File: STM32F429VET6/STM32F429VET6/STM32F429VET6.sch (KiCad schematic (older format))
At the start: 0 parts

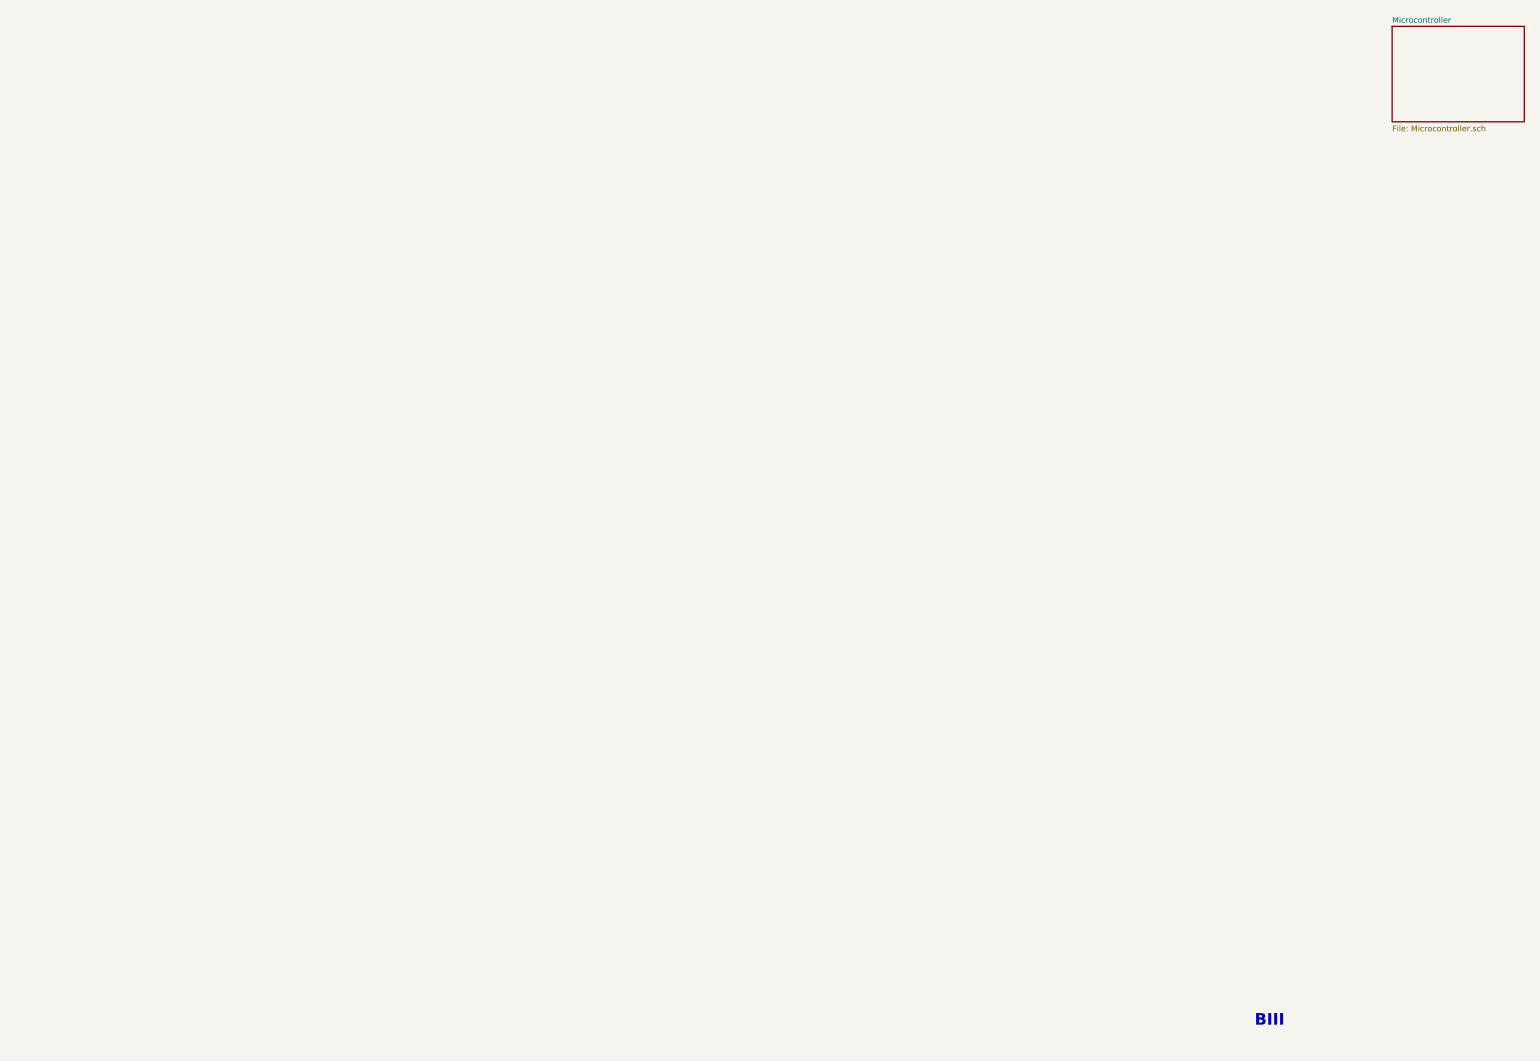
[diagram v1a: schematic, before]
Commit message: Completed Power Section
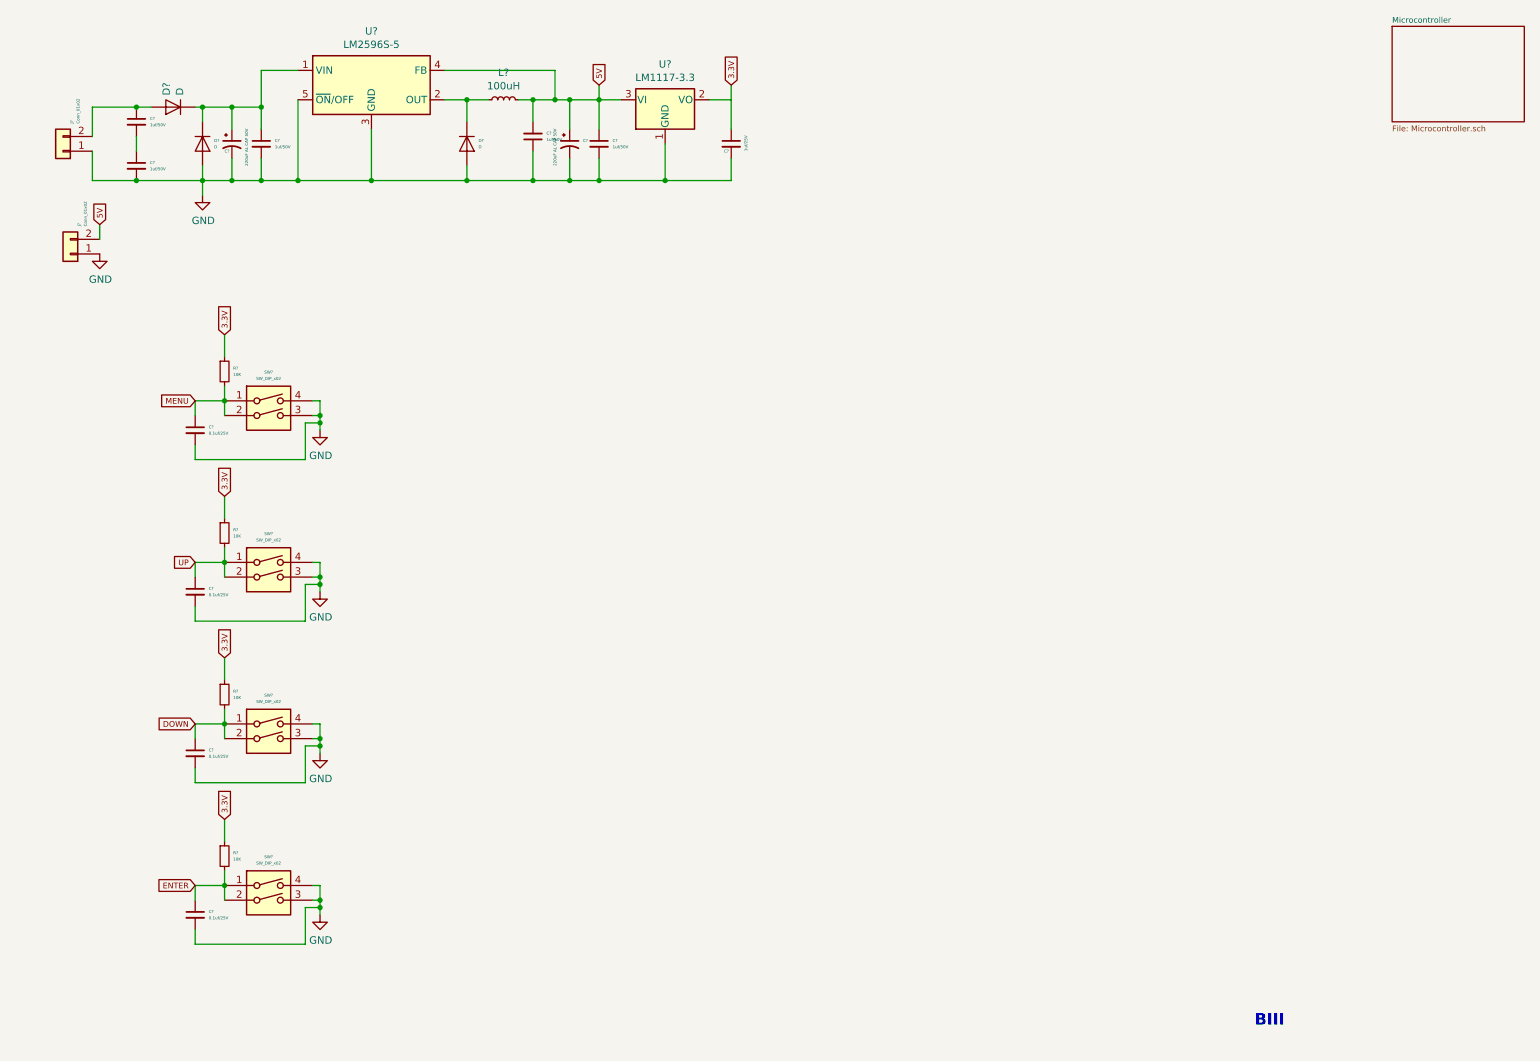
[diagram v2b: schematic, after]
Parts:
- added C? (x5): 1uf/50V, Capacitor_SMD:C_0805_2012Metric_Pad1.15x1.40mm_HandSolder, symbol Device:C_Small
- added C? (x2): 220uF AL CAP 50V, Capacitor_SMD:CP_Elec_4x4.5, symbol Device:CP1_Small
- added C?: 1uf/25V, Capacitor_SMD:C_0805_2012Metric_Pad1.15x1.40mm_HandSolder, symbol Device:C_Small
- added C? (x4): 0.1uf/25V, Capacitor_SMD:C_0805_2012Metric_Pad1.15x1.40mm_HandSolder, symbol Device:C_Small
- added D? (x3): D, symbol Device:D
- added J? (x2): Conn_01x02, Connector_PinHeader_2.54mm:PinHeader_1x02_P2.54mm_Vertical, symbol Connector_Generic:Conn_01x02
- added L?: 100uH, symbol Device:L_Small
- added R? (x4): 10K, Resistor_SMD:R_0805_2012Metric_Pad1.15x1.40mm_HandSolder, symbol Device:R_Small
- added SW? (x4): SW_DIP_x02, Button_Switch_SMD:SW_SPST_B3S-1000, symbol Switch:SW_DIP_x02
- added U?: LM2596S-5, Package_TO_SOT_SMD:TO-263-5_TabPin3, symbol Regulator_Switching:LM2596S-5
- added U?: LM1117-3.3, symbol Regulator_Linear:LM1117-3.3
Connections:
- new net: C?.1, D?.2 (A), J?.2 (Pin_2)
- new net: C?.1, C?.2
- new net: C?.1, C?.1, D?.1 (K), D?.1 (K), U?.1 (VIN)
- new net: D?.1 (K), L?.1, U?.2 (OUT)
- new net 3.3V: C?.1, R?.1, R?.1, R?.1, R?.1, U?.2 (VO)
- new net 5V: C?.1, C?.1, C?.2, J?.2 (Pin_2), L?.2, U?.3 (VI), U?.4 (FB)
- new net DOWN: C?.1, R?.2, SW?.1, SW?.2
- new net ENTER: C?.1, R?.2, SW?.1, SW?.2
- new net GND: C?.1, C?.2, C?.2, C?.2, C?.2, C?.2, C?.2, C?.2, C?.2, C?.2, C?.2, D?.2 (A), D?.2 (A), J?.1 (Pin_1), J?.1 (Pin_1), SW?.3, SW?.3, SW?.3, SW?.3, SW?.4, SW?.4, SW?.4, SW?.4, U?.1 (GND), U?.3 (GND), U?.5 (~ON~/OFF)
- new net MENU: C?.1, R?.2, SW?.1, SW?.2
- new net UP: C?.1, R?.2, SW?.1, SW?.2

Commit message: Completed 2 sections
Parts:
- added C?: 0.1uf/25V, Capacitor_SMD:C_0805_2012Metric_Pad1.15x1.40mm_HandSolder, symbol Device:C_Small
- added J?: Conn_01x03, symbol Connector_Generic:Conn_01x03
- added R? (x7): 10K, Resistor_SMD:R_0805_2012Metric_Pad1.15x1.40mm_HandSolder, symbol Device:R_Small
- added R? (x4): 100E, Resistor_SMD:R_0805_2012Metric_Pad1.15x1.40mm_HandSolder, symbol Device:R_Small
- added R? (x4): 10R, Resistor_SMD:R_0805_2012Metric_Pad1.15x1.40mm_HandSolder, symbol Device:R_Small
- added SW? (x12): SW_DIP_x02, Button_Switch_SMD:SW_SPST_B3S-1000, symbol Switch:SW_DIP_x02
- added U?: SN65HVD485ED, SN65HVD485ED:SN65HVD485ED, symbol SN65HVD485ED:SN65HVD485ED
- added U?: D5V0L2B3SO-7, D5V0L2B3SO7:D5V0L2B3SO-7, symbol D5V0L2B3SO7:D5V0L2B3SO-7
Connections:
- net 3.3V: now also R?.1, R?.1, R?.1, R?.1
- net 5V: now also C?.1, R?.1, R?.2, U?.8 (VCC)
- net GND: now also C?.2, J?.1 (Pin_1), R?.2, R?.2, U?.3 (EPAD), U?.5 (GND)
- new net: R?.1, R?.2, SW?.1, SW?.1, SW?.1, SW?.2, SW?.2, SW?.2 (x4)
- new net: R?.1, U?.6 (A)
- new net: R?.1, U?.7 (B)
- new net: J?.3 (Pin_3), R?.1, R?.1, R?.2, U?.1 (EPAD)
- new net: J?.2 (Pin_2), R?.1, R?.2, R?.2, U?.2 (EPAD)
- new net SW_CO1: SW?.3, SW?.3, SW?.3, SW?.3, SW?.4, SW?.4, SW?.4, SW?.4
- new net SW_CO2: SW?.3, SW?.3, SW?.3, SW?.3, SW?.4, SW?.4, SW?.4, SW?.4
- new net SW_CO3: SW?.3, SW?.3, SW?.3, SW?.3, SW?.4, SW?.4, SW?.4, SW?.4
- new net SW_RW1: R?.2
- new net SW_RW2: R?.2
- new net SW_RW3: R?.2
- new net SW_RW4: R?.2
- new net USART2_DE: R?.1, U?.2 (*RE), U?.3 (DE)
- new net USART2_RX: R?.2, U?.1 (R)
- new net USART2_TX: U?.4 (D)
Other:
- moved on the sheet: C?, R?, SW?

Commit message: Completed 3 pages
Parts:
- added C?: 0.1uf/25V, Capacitor_SMD:C_0805_2012Metric_Pad1.15x1.40mm_HandSolder, symbol Device:C_Small
- added R?: 10K, Resistor_SMD:R_0805_2012Metric_Pad1.15x1.40mm_HandSolder, symbol Device:R_Small
- added U?: T80-75HCP, symbol T80-75HCP:T80-75HCP
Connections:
- net 3.3V: now also C?.1, R?.1, U?.3 (WP#), U?.5 (VCC), U?.6 (HOLD)
- net GND: now also C?.2, U?.4 (VSS)
- new net SERIAL_FLASH_CLK: U?.7 (CLK)
- new net SERIAL_FLASH_CS: R?.2, U?.1 (CS#)
- new net SERIAL_FLASH_MISO: U?.2 (DO)
- new net SERIAL_FLASH_MOSI: U?.8 (DI)
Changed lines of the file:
@@
 	9700 3250 9200 3250
 Connection ~ 9200 3250
+$Comp
+L T80-75HCP:T80-75HCP U?
+U 1 1 5FD75780
+P 8500 5150
+F 0 "U?" H 8500 5475 50  0000 C CNN
+F 1 "T80-75HCP" H 8500 5384 50  0000 C CNN
+F 2 "" H 8500 5150 50  0001 C CNN
+F 3 "" H 8500 5150 50  0001 C CNN
+	1    8500 5150
+	1    0    0    -1
+$EndComp
+Wire Wire Line
+	7800 4850 7800 4800
+Text GLabel 7800 4700 1    39   Input ~ 0
+3.3V
+$Comp
+L Device:R_Small R?
+U 1 1 5FD84F8C
+P 7800 4950
+AR Path="/5FD5E119/5FD84F8C" Ref="R?"  Part="1"
+AR Path="/5FD84F8C" Ref="R?"  Part="1"
+F 0 "R?" H 7859 4972 20  0000 L CNN
+F 1 "10K" H 7859 4929 20  0000 L CNN
+F 2 "Resistor_SMD:R_0805_2012Metric_Pad1.15x1.40mm_HandSolder" H 7800 4950 50  0001 C CNN
+F 3 "~" H 7800 4950 50  0001 C CNN
+	1    7800 4950
+	1    0    0    -1
+$EndComp
+Wire Wire Line
+	8200 5050 7800 5050
+Text GLabel 8800 5350 2    39   Input ~ 0
+SERIAL_FLASH_MOSI
+Text GLabel 7500 5150 0    39   Input ~ 0
+SERIAL_FLASH_MISO
+Text GLabel 8800 5250 2    39   Input ~ 0
+SERIAL_FLASH_CLK
+Text GLabel 7450 5050 0    39   Input ~ 0
+SERIAL_FLASH_CS
+Wire Wire Line
+	7450 5050 7800 5050
+Connection ~ 7800 5050
+Wire Wire Line
+	7500 5150 8200 5150
+Wire Wire Line
+	8200 5250 7900 5250
+Wire Wire Line
+	7900 5250 7900 4800
+Wire Wire Line
+	7900 4800 7800 4800
+Connection ~ 7800 4800
+Wire Wire Line
+	7800 4800 7800 4700
+$Comp
+L power:GND #PWR?
+U 1 1 5FDFC7E1
+P 8200 5350
+AR Path="/5FD5E119/5FDFC7E1" Ref="#PWR?"  Part="1"
+AR Path="/5FDFC7E1" Ref="#PWR?"  Part="1"
+F 0 "#PWR?" H 8200 5100 50  0001 C CNN
+F 1 "GND" H 8205 5177 50  0000 C CNN
+F 2 "" H 8200 5350 50  0001 C CNN
+F 3 "" H 8200 5350 50  0001 C CNN
+	1    8200 5350
+	1    0    0    -1
+$EndComp
+Wire Wire Line
+	7900 4800 8800 4800
+Wire Wire Line
+	8800 4800 8800 5050
+Connection ~ 7900 4800
+Connection ~ 8800 5050
+Wire Wire Line
+	8800 5050 8800 5150
+$Comp
+L Device:C_Small C?
+U 1 1 5FE1BA0E
+P 9150 4800
+AR Path="/5FD5E119/5FE1BA0E" Ref="C?"  Part="1"
+AR Path="/5FE1BA0E" Ref="C?"  Part="1"
+F 0 "C?" H 9100 4750 20  0000 L CNN
+F 1 "0.1uf/25V" V 9250 4750 20  0000 L CNN
+F 2 "Capacitor_SMD:C_0805_2012Metric_Pad1.15x1.40mm_HandSolder" H 9150 4800 50  0001 C CNN
+F 3 "~" H 9150 4800 50  0001 C CNN
+	1    9150 4800
+	0    -1   -1   0
+$EndComp
+Connection ~ 8800 4800
+$Comp
+L power:GND #PWR?
+U 1 1 5FE49086
+P 9250 4800
+AR Path="/5FD5E119/5FE49086" Ref="#PWR?"  Part="1"
+AR Path="/5FE49086" Ref="#PWR?"  Part="1"
+F 0 "#PWR?" H 9250 4550 50  0001 C CNN
+F 1 "GND" H 9255 4627 50  0000 C CNN
+F 2 "" H 9250 4800 50  0001 C CNN
+F 3 "" H 9250 4800 50  0001 C CNN
+	1    9250 4800
+	0    -1   -1   0
+$EndComp
+Wire Wire Line
+	8800 4800 9050 4800
 $EndSCHEMATC

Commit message: Completed 4 pages
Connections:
- net 24V: now reaches C?.1, D?.2 (A), J?.2 (Pin_2)
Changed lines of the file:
@@
 $Descr A4 11693 8268
 encoding utf-8
-Sheet 1 2
+Sheet 1 3
 Title ""
 Date ""
@@
 	1100 1450 1100 1250
 Wire Wire Line
-	1100 1250 1400 1250
+	1100 1250 1200 1250
 Wire Wire Line
 	1100 1550 1100 1750
@@
 Wire Wire Line
 	8800 4800 9050 4800
+$Sheet
+S 8750 700  900  600
+U 5FE8625C
+F0 "Supporting_IC's" 50
+F1 "Supporting_IC's.sch" 50
+$EndSheet
+Text GLabel 1200 1150 1    39   Input ~ 0
+24V
+Wire Wire Line
+	1200 1250 1200 1150
+Connection ~ 1200 1250
+Wire Wire Line
+	1200 1250 1400 1250
 $EndSCHEMATC
